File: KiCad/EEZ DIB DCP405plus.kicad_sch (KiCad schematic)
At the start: 12 parts

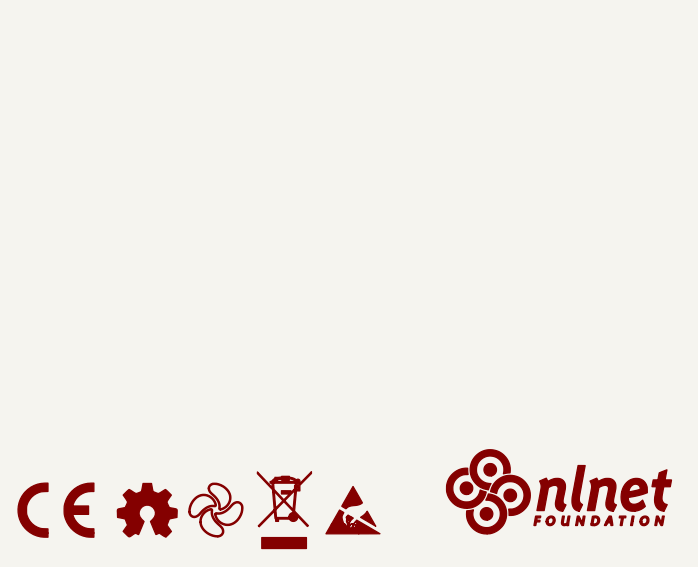
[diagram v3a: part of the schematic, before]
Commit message: Q18, Q19 model fixed
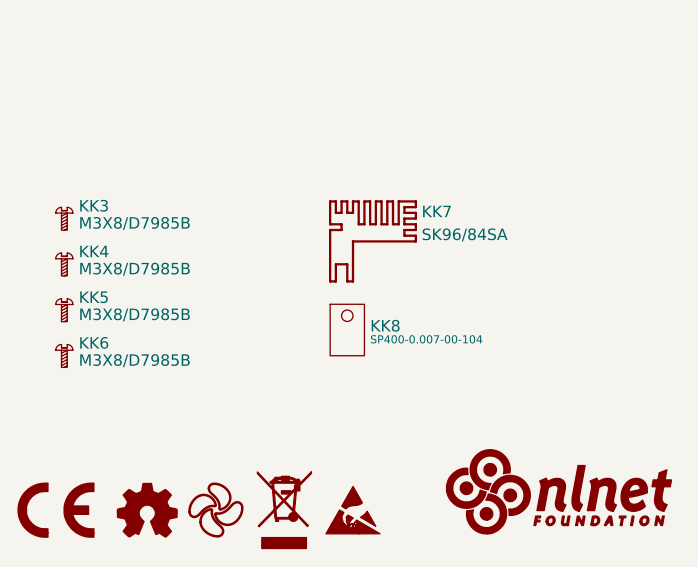
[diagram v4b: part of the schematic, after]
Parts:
- added KK3, KK4, KK5, KK6: M3X8/D7985B, symbol PCM_EEZ_unsorted:M3X8/D7985B
- added KK7: SK96/84SA, PCM_EEZ_unsorted:SK96_84, symbol PCM_EEZ_unsorted:SK96/84SA
- added KK8: SP400-0.007-00-104, symbol PCM_EEZ_unsorted:TO247_Thermal_pad

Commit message: #4
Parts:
- added KK10: B3/BN2842, symbol PCM_EEZ_unsorted:B3/BN2842
- added KK9: M3X8/D7985B, symbol PCM_EEZ_unsorted:M3X8/D7985B
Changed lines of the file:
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@@
 	(title_block
 		(title "${project_name}")
-		(date "2026-03-05")
+		(date "2026-03-22")
 		(rev "${project_version}")
 		(company "${project_creator}")
@@
 	)
 	(symbol
+		(lib_id "PCM_EEZ_unsorted:M3X8/D7985B")
+		(at 78.74 162.56 0)
+		(unit 1)
+		(exclude_from_sim no)
+		(in_bom yes)
+		(on_board no)
+		(dnp no)
+		(fields_autoplaced yes)
+		(property "Reference" "KK9"
+			(at 81.28 162.56 0)
+			(do_not_autoplace yes)
+			(effects
+				(font
+					(size 1.27 1.27)
+				)
+				(justify left bottom)
+			)
+		)
+		(property "Value" "M3X8/D7985B"
+			(at 81.28 164.465 0)
+			(do_not_autoplace yes)
+			(effects
+				(font
+					(size 1.27 1.27)
+				)
+				(justify left bottom)
+			)
+		)
+		(property "Footprint" ""
+			(at 78.74 162.56 0)
+			(effects
+				(font
+					(size 1.27 1.27)
+				)
+				(hide yes)
+			)
+		)
+		(property "Datasheet" ""
+			(at 78.74 162.56 0)
+			(effects
+				(font
+					(size 1.27 1.27)
+				)
+				(hide yes)
+			)
+		)
+		(property "Description" "Screw; M3x8; 0.5; Head: cheese head; Phillips; PH1; DIN 7985"
+			(at 78.74 165.1 0)
+			(effects
+				(font
+					(size 1.27 1.27)
+				)
+				(hide yes)
+			)
+		)
+		(property "DigiKey" "-"
+			(at 78.74 167.64 0)
+			(show_name yes)
+			(effects
+				(font
+					(size 1.27 1.27)
+				)
+				(hide yes)
+			)
+		)
+		(property "Mouser" "-"
+			(at 78.74 170.18 0)
+			(show_name yes)
+			(effects
+				(font
+					(size 1.27 1.27)
+				)
+				(hide yes)
+			)
+		)
+		(property "TME" "M3X8/D7985B"
+			(at 78.74 172.72 0)
+			(show_name yes)
+			(effects
+				(font
+					(size 1.27 1.27)
+				)
+				(hide yes)
+			)
+		)
+		(instances
+			(project "EEZ DIB DCP405plus"
+				(path "/65943c0e-8943-4d2a-93dc-fb4938f73312"
+					(reference "KK9")
+					(unit 1)
+				)
+			)
+		)
+	)
+	(symbol
 		(lib_id "PCM_EEZ_symbols:FIDUCIAL")
 		(at 154.94 190.5 0)
@@
 					(unit 1)
 				)
+			)
+		)
+	)
+	(symbol
+		(lib_id "PCM_EEZ_unsorted:B3/BN2842")
+		(at 79.375 157.48 0)
+		(unit 1)
+		(exclude_from_sim no)
+		(in_bom yes)
+		(on_board no)
+		(dnp no)
+		(property "Reference" "KK10"
+			(at 81.28 157.48 0)
+			(do_not_autoplace yes)
+			(effects
+				(font
+					(size 1.27 1.27)
+				)
+				(justify left bottom)
+			)
+		)
+		(property "Value" "B3/BN2842"
+			(at 81.28 159.385 0)
+			(do_not_autoplace yes)
+			(effects
+				(font
+					(size 1.27 1.27)
+				)
+				(justify left bottom)
+			)
+		)
+		(property "Footprint" ""
+			(at 79.375 157.48 0)
+			(effects
+				(font
+					(size 1.27 1.27)
+				)
+				(hide yes)
+			)
+		)
+		(property "Datasheet" ""
+			(at 79.375 157.48 0)
+			(effects
+				(font
+					(size 1.27 1.27)
+				)
+				(hide yes)
+			)
+		)
+		(property "Description" "Washer; externally serrated; M3"
+			(at 79.375 160.02 0)
+			(effects
+				(font
+					(size 1.27 1.27)
+				)
+				(hide yes)
+			)
+		)
+		(property "DigiKey" "-"
+			(at 79.375 162.56 0)
+			(show_name yes)
+			(effects
+				(font
+					(size 1.27 1.27)
+				)
+				(hide yes)
+			)
+		)
+		(property "Mouser" "-"
+			(at 79.375 165.1 0)
+			(show_name yes)
+			(effects
+				(font
+					(size 1.27 1.27)
+				)
+				(hide yes)
+			)
+		)
+		(property "TME" "B3/BN2842"
+			(at 79.375 167.64 0)
+			(show_name yes)
+			(effects
+				(font
+					(size 1.27 1.27)
+				)
+				(hide yes)
+			)
+		)
+		(instances
+			(project "EEZ DIB DCP405plus"
+				(path "/65943c0e-8943-4d2a-93dc-fb4938f73312"
+					(reference "KK10")
+					(unit 1)
+				)
